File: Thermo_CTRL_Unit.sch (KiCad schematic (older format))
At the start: 8 parts

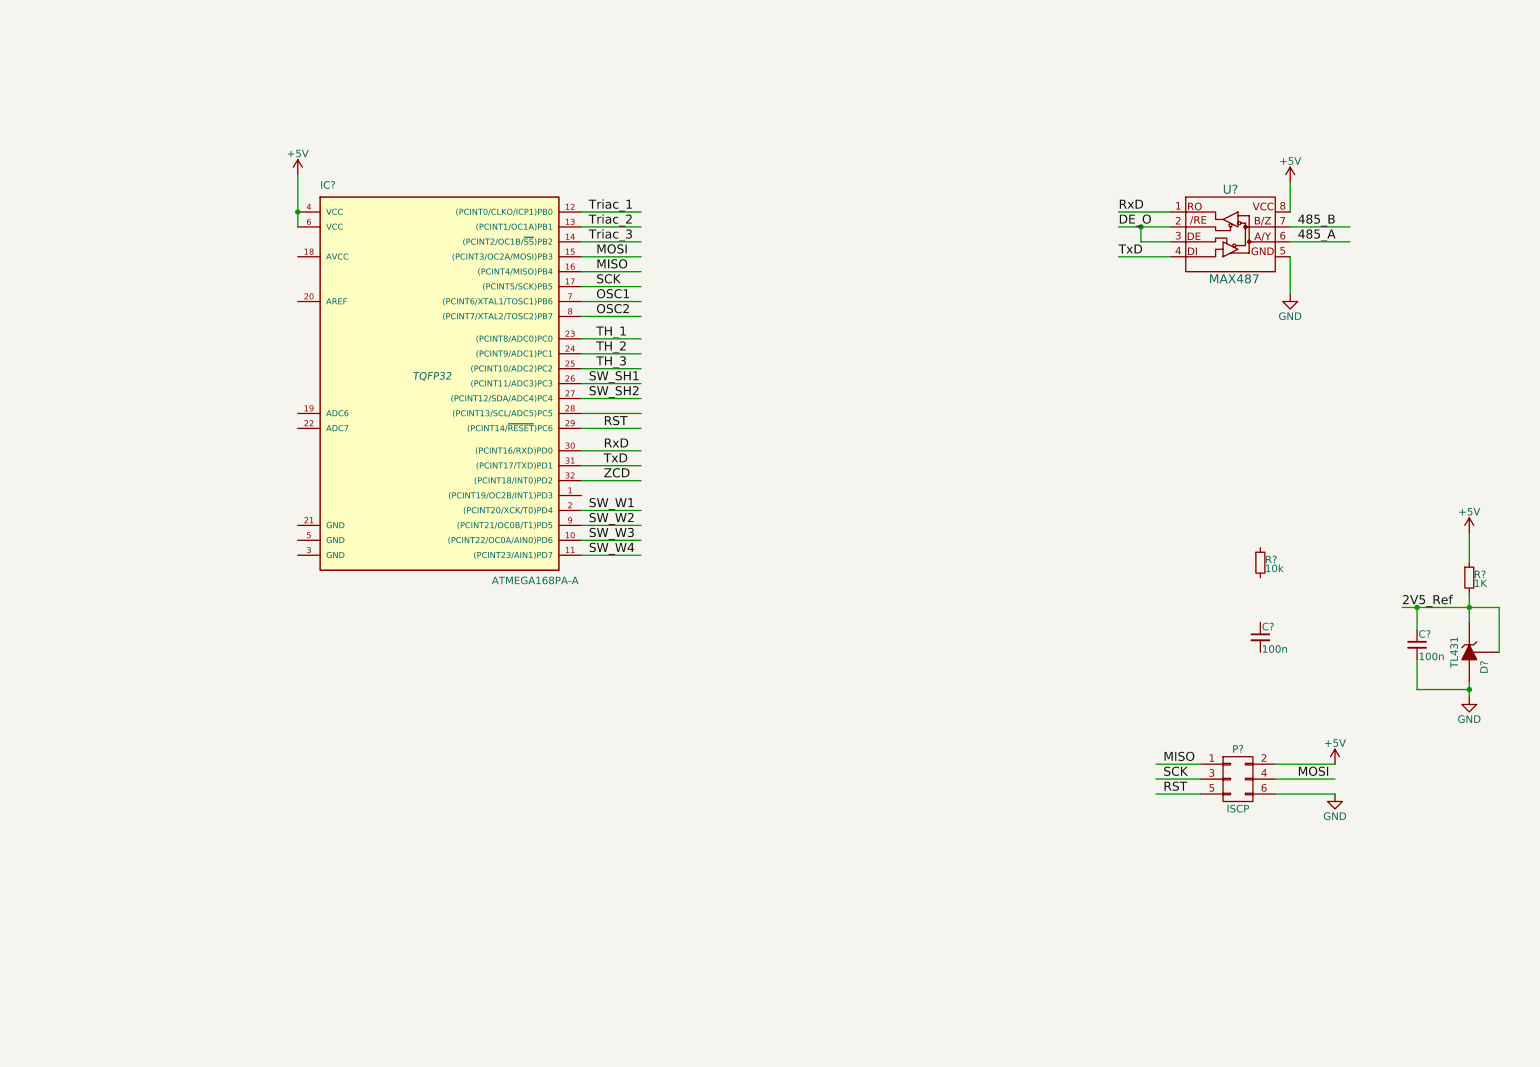
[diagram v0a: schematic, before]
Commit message: schematic update
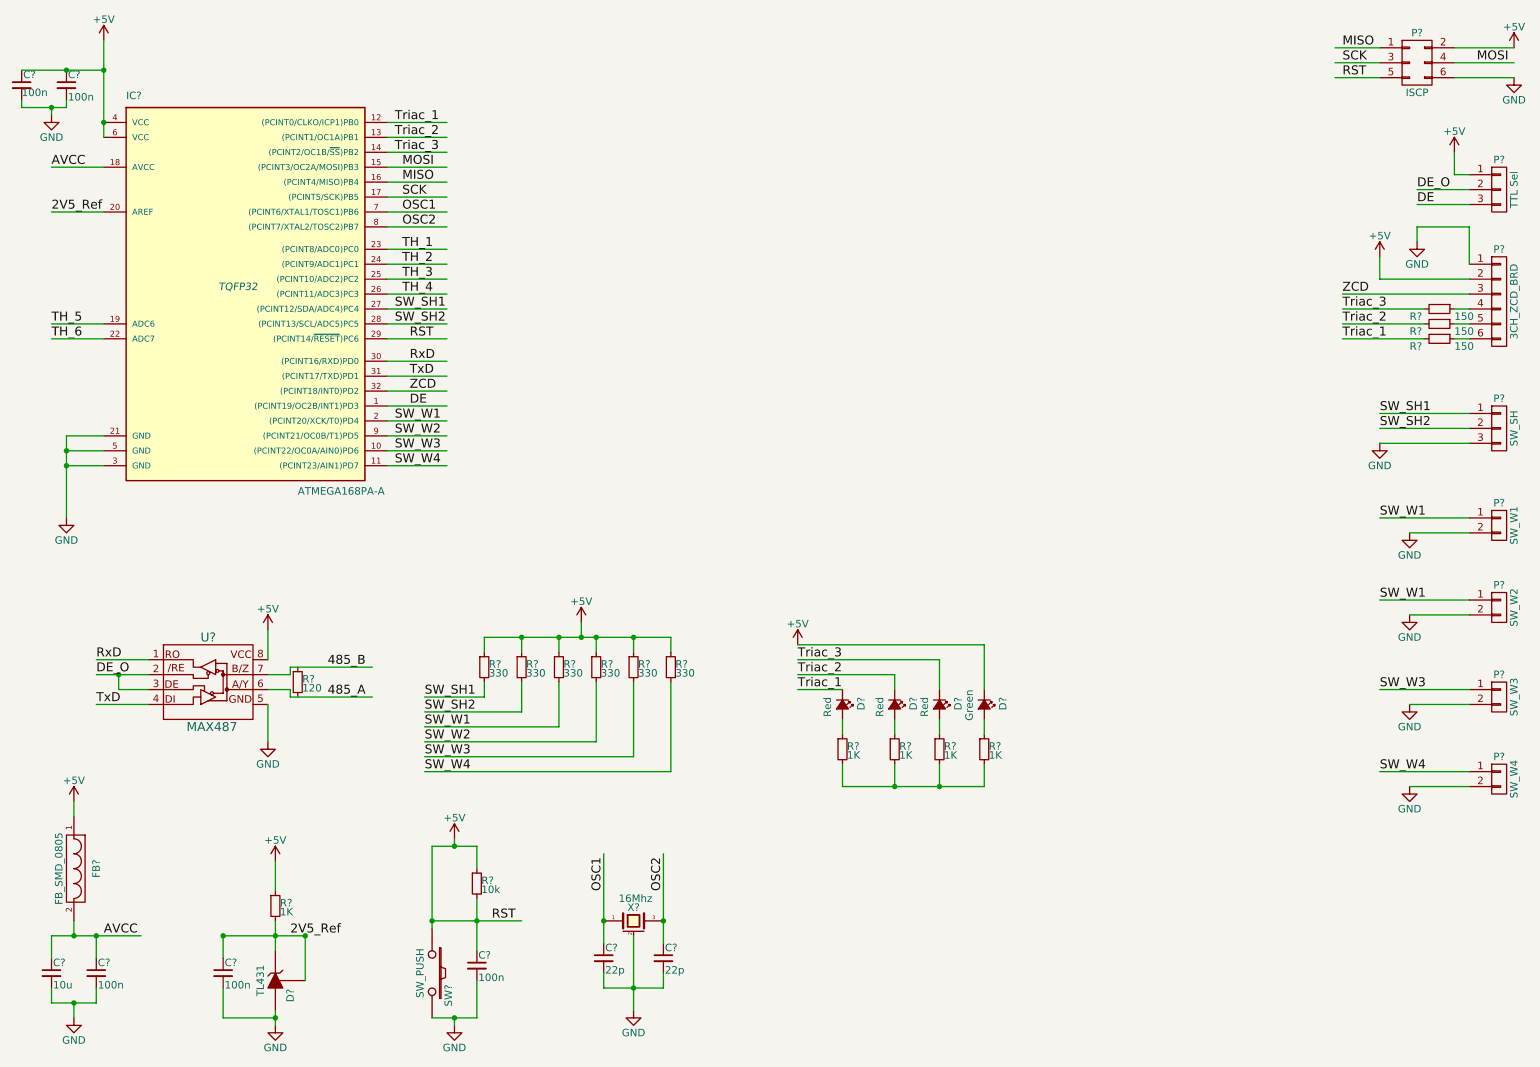
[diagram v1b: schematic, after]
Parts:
- added C? (x3): 100n, Capacitors_SMD:C_0805, symbol C_Cer_SMD_0805
- added C?: 10u, Capacitors_SMD:C_0805, symbol C_Cer_SMD_0805
- added C? (x2): 22p, Capacitors_SMD:C_0805, symbol C_Cer_SMD_0805
- added D? (x3): Red, symbol Led_Small
- added D?: Green, symbol Led_Small
- added FB?: FB_SMD_0805, Resistors_SMD:R_0805, symbol FB_SMD_0805
- added P?: 3CH_ZCD_BRD, symbol CONN_01X06
- added P?: TTL Sel, symbol CONN_01X03
- added P?: SW_SH, symbol CONN_01X03
- added P?: SW_W2, symbol CONN_01X02
- added P?: SW_W3, symbol CONN_01X02
- added P?: SW_W1, symbol CONN_01X02
- added P?: SW_W4, symbol CONN_01X02
- added R? (x4): 1K, Resistors_SMD:R_0805, symbol R_SMD_0805
- added R? (x3): 150, Resistors_SMD:R_0805, symbol R_SMD_0805
- added R? (x6): 330, Resistors_SMD:R_0805, symbol R_SMD_0805
- added R?: 120, Resistors_SMD:R_0805, symbol R_SMD_0805
- added SW?: SW_PUSH, BK_Common:SW_SPST_TACT_SMD_3X6, symbol SW_PUSH
- added X?: 16Mhz, BK_Common:crystal_smd_3225_4pin, symbol Chrystal_SMD_3225_4pin
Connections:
- net labels added: AVCC, DE, TH_4, TH_5, TH_6
- wire segments 46 -> 151
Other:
- moved on the sheet: C?, D?, IC?, P?, R?, U?

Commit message: PCB STRT
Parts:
- added C9: 100n, Capacitors_SMD:C_0805, symbol C_Cer_SMD_0805
- added J1: RJ12, BK_Common:RJ12_2mm_Pitch, symbol RJ12
- added P1: SW_TH1, BK_Common:JST_B3B-XH-A, symbol CONN_01X03
- added P10: SW_TH6, BK_Common:JST_B3B-XH-A, symbol CONN_01X03
- added P15: CONN_01X05, Pin_Headers:Pin_Header_Straight_1x05, symbol CONN_01X05
- added P3: SW_TH2, BK_Common:JST_B3B-XH-A, symbol CONN_01X03
- added P5: SW_TH3, BK_Common:JST_B3B-XH-A, symbol CONN_01X03
- added P7: SW_TH4, BK_Common:JST_B3B-XH-A, symbol CONN_01X03
- added P8: SW_TH5, BK_Common:JST_B3B-XH-A, symbol CONN_01X03
- D1, D2, D3, D4: renamed from D?; footprint (none) -> LEDs:LED_0805
- IC1: renamed from IC?; footprint TQFP32 -> Housings_QFP:TQFP-32_7x7mm_Pitch0.8mm
- P11, P12, P13, P14: renamed from P?; footprint (none) -> BK_Common:JST_B2B-XH-A
- P2: renamed from P?; footprint (none) -> Pin_Headers:Pin_Header_Straight_2x03
- P4: renamed from P?; footprint (none) -> Pin_Headers:Pin_Header_Straight_1x03
- P6: renamed from P?; footprint (none) -> Pin_Headers:Pin_Header_Straight_1x06
- P9: renamed from P?; footprint (none) -> Terminal_Blocks:TerminalBlock_Pheonix_MKDS1.5-3pol
- gave numbers to parts that had none: 29
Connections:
- net labels added: DTR
- wire segments 151 -> 183
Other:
- moved on the sheet: D1, D2, D3, D4, R10, R11, R12, R13, R14, R4, R5, R6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

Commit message: PCB Update
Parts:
- removed P10: SW_TH6, BK_Common:JST_B3B-XH-A, symbol CONN_01X03
- removed P8: SW_TH5, BK_Common:JST_B3B-XH-A, symbol CONN_01X03
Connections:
- net labels added: SCL, SDA
- net labels removed: TH_5, TH_6
- wire segments 183 -> 178
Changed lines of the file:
@@
 Text Label 3350 2350 0    60   ~ 0
 TH_2
-Text Label 3350 2450 0    60   ~ 0
+Text Label 1000 2750 0    60   ~ 0
 TH_3
 Text Label 3400 3200 0    60   ~ 0
@@
 Text Label 3300 3700 0    60   ~ 0
 SW_W4
-Text Label 3300 2650 0    60   ~ 0
+Text Label 3300 2450 0    60   ~ 0
 SW_SH1
-Text Label 3300 2750 0    60   ~ 0
+Text Label 3300 2550 0    60   ~ 0
 SW_SH2
 $Comp
@@
 Text Label 1000 2000 0    60   ~ 0
 2V5_Ref
-Text Label 3350 2550 0    60   ~ 0
+Text Label 1000 2850 0    60   ~ 0
 TH_4
-Text Label 1000 2750 0    60   ~ 0
-TH_5
-Text Label 1000 2850 0    60   ~ 0
-TH_6
 Wire Wire Line
 	5450 2250 5250 2250
@@
 L GND #PWR013
 U 1 1 56EA9D18
-P 4900 7350
-F 0 "#PWR013" H 4900 7100 50  0001 C CNN
-F 1 "GND" H 4900 7200 50  0000 C CNN
-F 2 "" H 4900 7350 50  0000 C CNN
-F 3 "" H 4900 7350 50  0000 C CNN
-	1    4900 7350
+P 4700 5750
+F 0 "#PWR013" H 4700 5500 50  0001 C CNN
+F 1 "GND" H 4700 5600 50  0000 C CNN
+F 2 "" H 4700 5750 50  0000 C CNN
+F 3 "" H 4700 5750 50  0000 C CNN
+	1    4700 5750
 	1    0    0    -1
 $EndComp
@@
 TH_4
 $Comp
-L CONN_01X03 P8
-U 1 1 56EBB3F8
-P 8950 4100
-F 0 "P8" H 8950 4300 50  0000 C CNN
-F 1 "SW_TH5" V 9050 4100 50  0000 C CNN
-F 2 "BK_Common:JST_B3B-XH-A" H 8950 4100 50  0001 C CNN
-F 3 "" H 8950 4100 50  0000 C CNN
-	1    8950 4100
-	1    0    0    -1
-$EndComp
-Wire Wire Line
-	8750 4000 8150 4000
-Wire Wire Line
-	8750 4100 8150 4100
-Wire Wire Line
-	8750 4200 8150 4200
-$Comp
-L GND #PWR032
-U 1 1 56EBB401
-P 8150 4200
-F 0 "#PWR032" H 8150 3950 50  0001 C CNN
-F 1 "GND" H 8150 4050 50  0000 C CNN
-F 2 "" H 8150 4200 50  0000 C CNN
-F 3 "" H 8150 4200 50  0000 C CNN
-	1    8150 4200
-	1    0    0    -1
-$EndComp
-$Comp
-L +5V #PWR033
-U 1 1 56EBB407
-P 8150 4000
-F 0 "#PWR033" H 8150 3850 50  0001 C CNN
-F 1 "+5V" H 8150 4140 50  0000 C CNN
-F 2 "" H 8150 4000 50  0000 C CNN
-F 3 "" H 8150 4000 50  0000 C CNN
-	1    8150 4000
-	1    0    0    -1
-$EndComp
-Text Label 8150 4100 0    60   ~ 0
-TH_5
-$Comp
-L CONN_01X03 P10
-U 1 1 56EBB539
-P 8950 4700
-F 0 "P10" H 8950 4900 50  0000 C CNN
-F 1 "SW_TH6" V 9050 4700 50  0000 C CNN
-F 2 "BK_Common:JST_B3B-XH-A" H 8950 4700 50  0001 C CNN
-F 3 "" H 8950 4700 50  0000 C CNN
-	1    8950 4700
-	1    0    0    -1
-$EndComp
-Wire Wire Line
-	8750 4600 8150 4600
-Wire Wire Line
-	8750 4700 8150 4700
-Wire Wire Line
-	8750 4800 8150 4800
-$Comp
-L GND #PWR034
-U 1 1 56EBB542
-P 8150 4800
-F 0 "#PWR034" H 8150 4550 50  0001 C CNN
-F 1 "GND" H 8150 4650 50  0000 C CNN
-F 2 "" H 8150 4800 50  0000 C CNN
-F 3 "" H 8150 4800 50  0000 C CNN
-	1    8150 4800
-	1    0    0    -1
-$EndComp
-$Comp
-L +5V #PWR035
-U 1 1 56EBB548
-P 8150 4600
-F 0 "#PWR035" H 8150 4450 50  0001 C CNN
-F 1 "+5V" H 8150 4740 50  0000 C CNN
-F 2 "" H 8150 4600 50  0000 C CNN
-F 3 "" H 8150 4600 50  0000 C CNN
-	1    8150 4600
-	1    0    0    -1
-$EndComp
-Text Label 8150 4700 0    60   ~ 0
-TH_6
-$Comp
 L RJ12 J1
 U 1 1 56EC3AC3
@@
 	5200 3250 5200 3450
 $Comp
-L GND #PWR036
+L GND #PWR032
 U 1 1 56EC40AB
 P 5200 3450
-F 0 "#PWR036" H 5200 3200 50  0001 C CNN
+F 0 "#PWR032" H 5200 3200 50  0001 C CNN
 F 1 "GND" H 5200 3300 50  0000 C CNN
 F 2 "" H 5200 3450 50  0000 C CNN
@@
 	5650 3550 5800 3550
 $Comp
-L +5V #PWR037
+L +5V #PWR033
 U 1 1 56EC443F
 P 5500 3700
-F 0 "#PWR037" H 5500 3550 50  0001 C CNN
+F 0 "#PWR033" H 5500 3550 50  0001 C CNN
 F 1 "+5V" H 5500 3840 50  0000 C CNN
 F 2 "" H 5500 3700 50  0000 C CNN
@@
 $EndComp
 $Comp
-L +5V #PWR038
+L +5V #PWR034
 U 1 1 56ED108E
 P 6100 6700
-F 0 "#PWR038" H 6100 6550 50  0001 C CNN
+F 0 "#PWR034" H 6100 6550 50  0001 C CNN
 F 1 "+5V" H 6100 6840 50  0000 C CNN
 F 2 "" H 6100 6700 50  0000 C CNN
@@
 $EndComp
 $Comp
-L GND #PWR039
+L GND #PWR035
 U 1 1 56ED112F
 P 6100 7200
-F 0 "#PWR039" H 6100 6950 50  0001 C CNN
+F 0 "#PWR035" H 6100 6950 50  0001 C CNN
 F 1 "GND" H 6100 7050 50  0000 C CNN
 F 2 "" H 6100 7200 50  0000 C CNN
@@
 Text Label 5900 6950 0    60   ~ 0
 TxD
+Text Label 3400 2650 0    60   ~ 0
+SDA
+Text Label 3400 2750 0    60   ~ 0
+SCL
+$Comp
+L GND #PWR036
+U 1 1 56EBFC1A
+P 4900 7350
+F 0 "#PWR036" H 4900 7100 50  0001 C CNN
+F 1 "GND" H 4900 7200 50  0000 C CNN
+F 2 "" H 4900 7350 50  0000 C CNN
+F 3 "" H 4900 7350 50  0000 C CNN
+	1    4900 7350
+	1    0    0    -1
+$EndComp
+Wire Wire Line
+	4700 5750 4700 5700
+Connection ~ 4700 5700
 $EndSCHEMATC

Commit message: SCH change
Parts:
- added C10, C13: 10uF, Capacitors_SMD:C_1206, symbol C_Cer_SMD_1206
- added C11: 100nF, Capacitors_SMD:C_0805, symbol C_Cer_SMD_0805
- added C12: 1uF, Capacitors_SMD:C_1206, symbol C_Cer_SMD_1206
- added D6: SS13, Diodes_SMD:SMA_Standard, symbol SS13
- added P10: IIC, Pin_Headers:Pin_Header_Straight_1x04, symbol CONN_01X04
- added P8: VIN, Pin_Headers:Pin_Header_Straight_1x02, symbol CONN_01X02
- added R17, R18: 1K, Resistors_SMD:R_0805, symbol R_SMD_0805
- added U2: MC78M05CDT, TO_SOT_Packages_SMD:TO-252-2Lead, symbol MC78M05CDT
- added U3: HT7333-A, TO_SOT_Packages_SMD:SOT89-3_Housing, symbol HT7333-A
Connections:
- net labels added: +3.3V, VIN
- wire segments 178 -> 204
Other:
- moved on the sheet: D1, D2, D3, D4, J1, P1, P3, P5, P7, R10, R11, R12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

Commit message: PCB Change
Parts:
- C1: value 100n -> 1u
